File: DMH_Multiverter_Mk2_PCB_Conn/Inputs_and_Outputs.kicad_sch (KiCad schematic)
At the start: 25 parts, among them J1 TS_Jack_6.35mm_Sw, J10 TS_Jack_6.35mm_Sw, J11 TS_Jack_6.35mm_Sw, J12 TS_Jack_6.35mm_Sw, J13 TS_Jack_6.35mm_Sw, J14 TS_Jack_6.35mm_Sw, J15 TS_Jack_6.35mm_Sw, J16 TS_Jack_6.35mm_Sw, J17 TS_Jack_6.35mm_Sw, J18 TS_Jack_6.35mm_Sw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

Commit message: pcb 2 in progress
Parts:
- removed J16, J17, J18, J19, J20, J21, J22: TS_Jack_6.35mm_Sw, SynthStuff:CUI_MJ-63052A, symbol SynthStuff:TS_Jack_6.35mm_Sw
- removed J50, J60: Conn_01x06, Connector_PinHeader_2.54mm:PinHeader_1x06_P2.54mm_Vertical, symbol Connector_Generic:Conn_01x06
- added D3: ZPD5V1, Diode_THT:D_DO-35_SOD27_P7.62mm_Horizontal, symbol Diode:ZPDxx
- added J50, J60: Conn_01x08, Connector_PinHeader_2.54mm:PinHeader_1x08_P2.54mm_Vertical, symbol Connector_Generic:Conn_01x08
- added R7: 10k, Resistor_THT:R_Axial_DIN0207_L6.3mm_D2.5mm_P7.62mm_Horizontal, symbol Device:R_US
- J1: Function Att A In -> Att A Input
- J10: Function M 2 Out 2 -> Mult 2 Input
- J11: Function Mult 3 In -> Mult 2 Output 1
- J12: Function M 3 Out 1 -> Mult 2 Output 2
- J13: Function M 3 Out 2 -> Mult 3 Input
- J14: Function Mult 4 In -> Mult 3 Output 1
- J15: Function M 4 Out 1 -> Mult 3 Output 2
- J2: Function Att A Out -> Att A Output
- J3: Function Att B In -> Att B Input
- J4: Function Att B Out -> Att B Output
- J5: Function Mult 1 In -> Att C Input
- J6: Function M 1 Out 1 -> Att C Output
- J7: Function M 1 Out 2 -> Mult 1 Input
- J8: Function Mult 2 In -> Mult 1 Output 1
- J9: Function M 2 Out 1 -> Mult 1 Output 2
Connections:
- net Att A Input Jack: now also J50.1 (Pin_1)
- net Att A Output Jack: now also J50.2 (Pin_2)
- net Att B Input Jack: now also J50.3 (Pin_3)
- net Att B Output Jack: now also J50.4 (Pin_4)
- net GND: now also J200.3 (Pin_3), D3.2 (A), J50.7 (Pin_7), J50.8 (Pin_8), J60.7 (Pin_7), J60.8 (Pin_8); no longer J200.5 (Pin_5)
- net at J1.TN: now also J3.TN, J5.TN, D3.1 (K), J60.1 (Pin_1), J60.3 (Pin_3), J60.5 (Pin_5), R7.1; no longer J200.1 (Pin_1)
- net at J2.TN: now also J200.1 (Pin_1), J200.4 (Pin_4), J60.2 (Pin_2); no longer J200.2 (Pin_2)
- net at J4.TN: now also J200.2 (Pin_2), J60.4 (Pin_4); no longer J200.4 (Pin_4)
- net at J11.T, J12.T: now also J10.T, J13.TN; no longer J13.T, J14.TN
- net at J8.T, J9.T: now also J10.TN, J7.T; no longer J10.T, J11.TN
- net at J6.TN: now also J200.5 (Pin_5), J60.6 (Pin_6)
- net at J14.T, J15.T: now also J13.T
- new net +12V: R7.2
- new net Att C Input Jack: J5.T, J50.5 (Pin_5)
- new net Att C Output Jack: J50.6 (Pin_6), J6.T
- now unconnected: J8.TN
- no-connect marks 13 -> 7

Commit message: Routed Connectors PCB
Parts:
- J50, J60: footprint Connector_PinHeader_2.54mm:PinHeader_1x08_P2.54mm_Vertical -> Connector_PinSocket_2.54mm:PinSocket_1x08_P2.54mm_Vertical
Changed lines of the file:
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@@
 			)
 		)
-		(property "Footprint" "Connector_PinHeader_2.54mm:PinHeader_1x08_P2.54mm_Vertical"
+		(property "Footprint" "Connector_PinSocket_2.54mm:PinSocket_1x08_P2.54mm_Vertical"
 			(at 88.9 147.32 0)
 			(effects
@@
 			)
 		)
-		(property "Footprint" "Connector_PinHeader_2.54mm:PinHeader_1x08_P2.54mm_Vertical"
+		(property "Footprint" "Connector_PinSocket_2.54mm:PinSocket_1x08_P2.54mm_Vertical"
 			(at 88.9 175.26 0)
 			(effects
@@
 			)
 		)
+		(property "Function" ""
+			(at 88.9 175.26 0)
+			(effects
+				(font
+					(size 1.27 1.27)
+				)
+			)
+		)

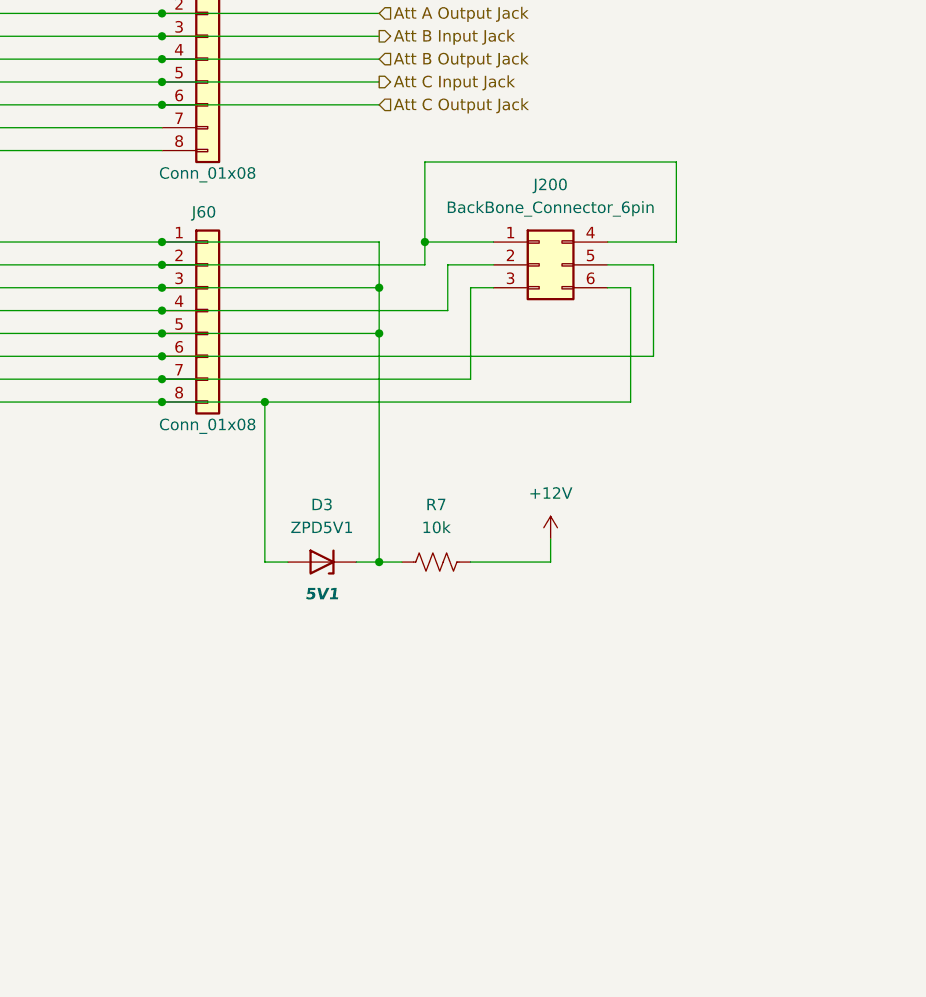
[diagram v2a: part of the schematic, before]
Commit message: Independent zeners for normalled 5V DC offset
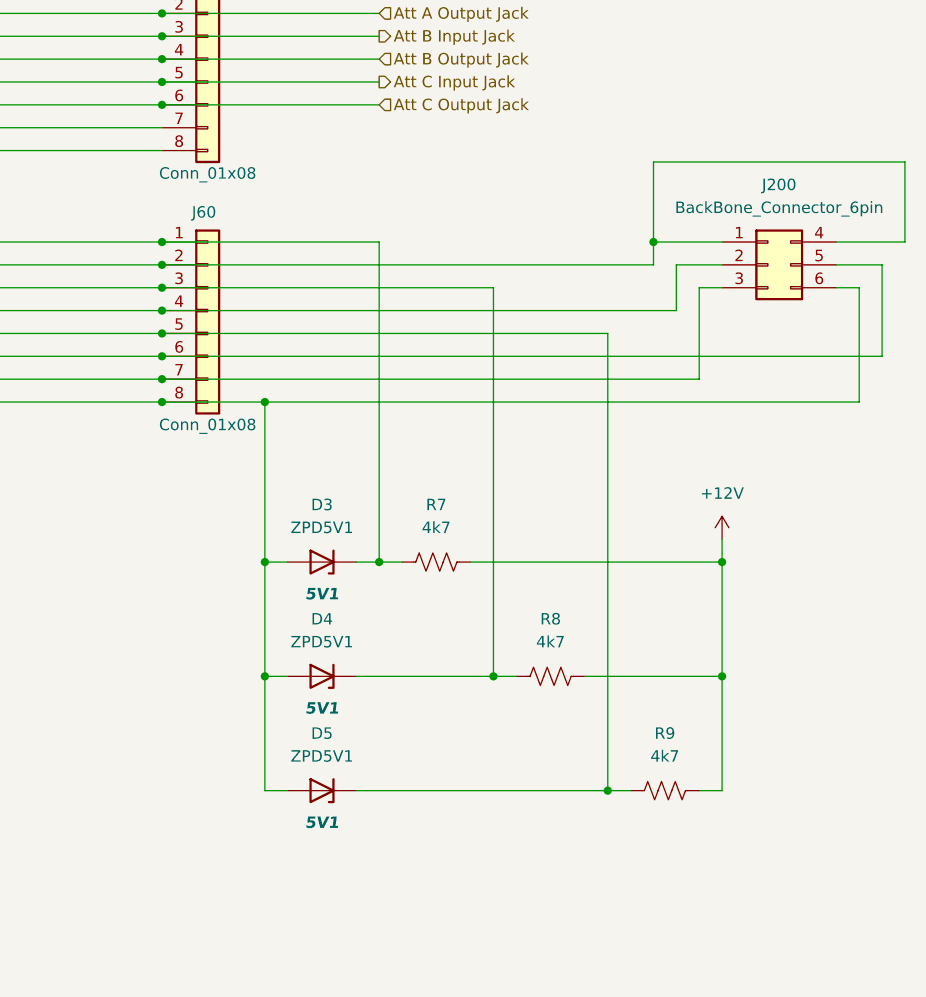
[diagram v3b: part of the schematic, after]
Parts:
- added D4, D5: ZPD5V1, Diode_THT:D_DO-35_SOD27_P7.62mm_Horizontal, symbol Diode:ZPDxx
- added R8, R9: 4k7, Resistor_THT:R_Axial_DIN0207_L6.3mm_D2.5mm_P7.62mm_Horizontal, symbol Device:R_US
- R7: value 10k -> 4k7
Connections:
- net +12V: now also R8.2, R9.2
- net GND: now also D4.2 (A), D5.2 (A)
- net at D3.1 (K), J1.TN, J60.1 (Pin_1)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: no longer J3.TN, J5.TN, J60.3 (Pin_3), J60.5 (Pin_5)
- new net: D5.1 (K), J5.TN, J60.5 (Pin_5), R9.1
- new net: D4.1 (K), J3.TN, J60.3 (Pin_3), R8.1
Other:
- moved on the sheet: J200
